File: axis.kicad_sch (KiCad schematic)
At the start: 43 parts, among them J101 CORTEX-DEBUG, J102 JAE_DX07S016JA3, SW101 SW_Push, SW102 SW_Push, U101 TPS78433QWDRBRQ1, U102 ATSAMD51G, U103 BMM150, U104 BHI160, Y101 32k768

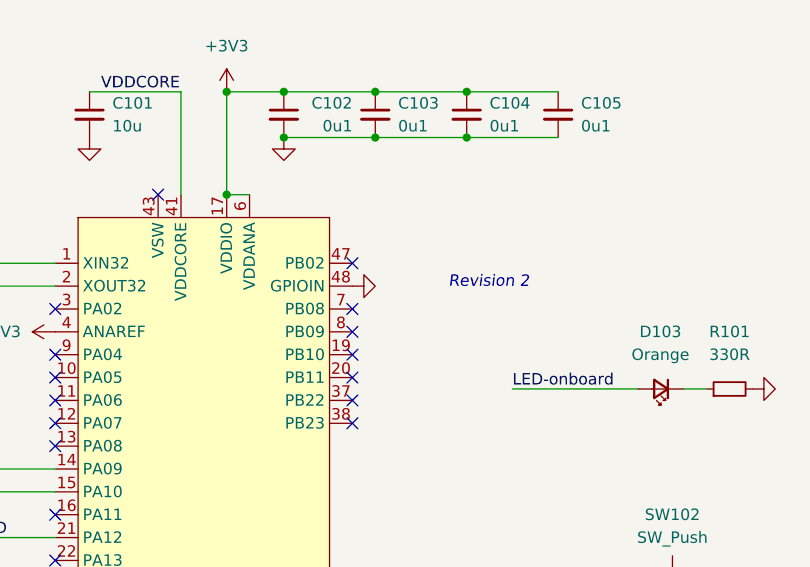
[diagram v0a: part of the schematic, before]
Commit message: Remove revision pin
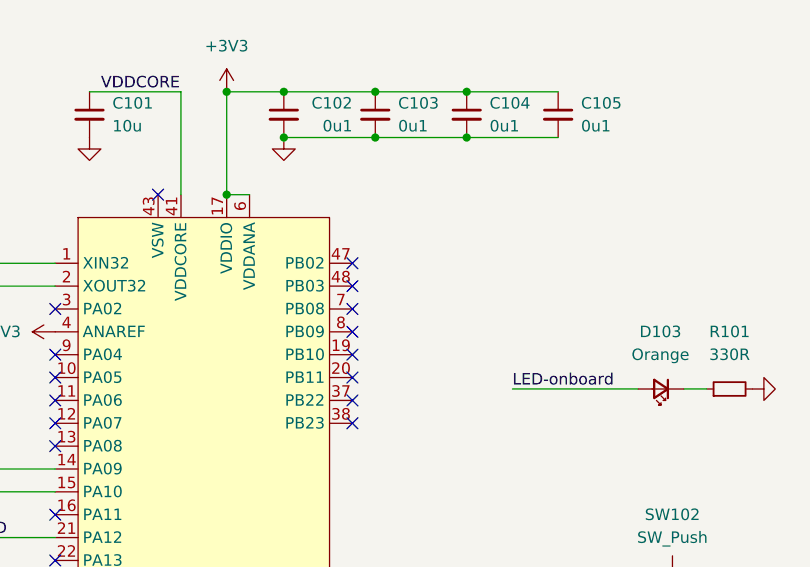
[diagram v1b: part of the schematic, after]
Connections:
- net GND: no longer U102.48 (PB03)
- no-connect marks 29 -> 30
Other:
- note removed: "Revision 2"
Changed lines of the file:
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@@
 		)
 	)
-	(text "Revision 2"
-		(exclude_from_sim no)
-		(at 103.3812 43.5526 0)
-		(effects
-			(font
-				(size 1.27 1.27)
-				(italic yes)
-			)
-			(justify left bottom)
-		)
-	)
 	(text "Mechanical / Production"
 		(exclude_from_sim no)
@@
 	)
 	(no_connect
+		(at 92.71 43.18)
+	)
+	(no_connect
 		(at 71.12 33.02)
 	)
@@
 	(symbol
 		(lib_id "power:GND")
-		(at 92.71 43.18 90)
-		(unit 1)
-		(exclude_from_sim no)
-		(in_bom yes)
-		(on_board yes)
-		(dnp no)
-		(property "Reference" "#PWR0107"
-			(at 99.06 43.18 0)
-			(effects
-				(font
-					(size 1.27 1.27)
-				)
-				(hide yes)
-			)
-		)
-		(property "Value" "GND"
-			(at 96.52 42.5449 90)
-			(effects
-				(font
-					(size 1.27 1.27)
-				)
-				(justify right)
-				(hide yes)
-			)
-		)
-		(property "Footprint" ""
-			(at 92.71 43.18 0)
-			(effects
-				(font
-					(size 1.27 1.27)
-				)
-				(hide yes)
-			)
-		)
-		(property "Datasheet" ""
-			(at 92.71 43.18 0)
-			(effects
-				(font
-					(size 1.27 1.27)
-				)
-				(hide yes)
-			)
-		)
-		(property "Description" ""
-			(at 92.71 43.18 0)
-			(effects
-				(font
-					(size 1.27 1.27)
-				)
-				(hide yes)
-			)
-		)
-		(pin "1"
-		)
-		(instances
-			(project "axis"
-				(path "/6c8448b4-b04d-47e1-934e-e40cbe27a7be"
-					(reference "#PWR0107")
-					(unit 1)
-				)
-			)
-		)
-	)
-	(symbol
-		(lib_id "power:GND")
 		(at 215.9 97.79 90)
 		(unit 1)
@@
 			)
 		)
+		(property "Sim.Pins" "1=K 2=A"
+			(at 127 54.61 0)
+			(effects
+				(font
+					(size 1.27 1.27)
+				)
+				(hide yes)
+			)
+		)
 		(pin "1"
 		)
@@
 		(at 205.74 157.48 90)
 		(unit 1)
-		(exclude_from_sim yes)
+		(exclude_from_sim no)
 		(in_bom no)
 		(on_board yes)
@@
 			)
 		)
+		(property "Sim.Enable" "0"
+			(at 205.74 157.48 0)
+			(effects
+				(font
+					(size 1.27 1.27)
+				)
+				(hide yes)
+			)
+		)
 		(instances
 			(project "axis"
@@
 		(at 247.65 151.13 0)
 		(unit 1)
-		(exclude_from_sim yes)
+		(exclude_from_sim no)
 		(in_bom no)
 		(on_board yes)
@@
 			)
 		)
+		(property "Sim.Enable" "0"
+			(at 247.65 151.13 0)
+			(effects
+				(font
+					(size 1.27 1.27)
+				)
+				(hide yes)
+			)
+		)
 		(instances
 			(project ""
@@
 		(at 125.73 101.6 0)
 		(unit 1)
-		(exclude_from_sim yes)
+		(exclude_from_sim no)
 		(in_bom no)
 		(on_board yes)
@@
 			)
 		)
+		(property "Sim.Enable" "0"
+			(at 125.73 101.6 0)
+			(effects
+				(font
+					(size 1.27 1.27)
+				)
+				(hide yes)
+			)
+		)
 		(pin "1"
 		)
@@
 		(at 180.34 189.23 0)
 		(unit 1)
-		(exclude_from_sim yes)
+		(exclude_from_sim no)
 		(in_bom no)
 		(on_board yes)
@@
 			)
 		)
+		(property "Sim.Enable" "0"
+			(at 180.34 189.23 0)
+			(effects
+				(font
+					(size 1.27 1.27)
+				)
+				(hide yes)
+			)
+		)
 		(instances
 			(project "axis"
@@
 		(at 232.41 157.48 0)
 		(unit 1)
-		(exclude_from_sim yes)
+		(exclude_from_sim no)
 		(in_bom no)
 		(on_board yes)
@@
 			)
 		)
+		(property "Sim.Enable" "0"
+			(at 232.41 157.48 0)
+			(effects
+				(font
+					(size 1.27 1.27)
+				)
+				(hide yes)
+			)
+		)
 		(instances
 			(project "axis"
@@
 		(at 134.62 171.45 0)
 		(unit 1)
-		(exclude_from_sim yes)
+		(exclude_from_sim no)
 		(in_bom yes)
 		(on_board yes)
@@
 			)
 		)
+		(property "Sim.Enable" "0"
+			(at 134.62 171.45 0)
+			(effects
+				(font
+					(size 1.27 1.27)
+				)
+				(hide yes)
+			)
+		)
 		(pin "A1"
 		)
@@
 		(at 276.86 154.94 0)
 		(unit 1)
-		(exclude_from_sim yes)
+		(exclude_from_sim no)
 		(in_bom no)
 		(on_board yes)
@@
 			)
 		)
+		(property "Sim.Enable" "0"
+			(at 276.86 154.94 0)
+			(effects
+				(font
+					(size 1.27 1.27)
+				)
+				(hide yes)
+			)
+		)
 		(instances
 			(project "axis"
@@
 		(at 276.86 166.37 0)
 		(unit 1)
-		(exclude_from_sim yes)
+		(exclude_from_sim no)
 		(in_bom no)
 		(on_board yes)
@@
 			)
 		)
+		(property "Sim.Enable" "0"
+			(at 276.86 166.37 0)
+			(effects
+				(font
+					(size 1.27 1.27)
+				)
+				(hide yes)
+			)
+		)
 		(instances
 			(project "axis"
@@
 		(at 49.53 173.99 0)
 		(unit 1)
-		(exclude_from_sim yes)
+		(exclude_from_sim no)
 		(in_bom yes)
 		(on_board yes)
@@
 			)
 		)
+		(property "Sim.Enable" "0"
+			(at 49.53 173.99 0)
+			(effects
+				(font
+					(size 1.27 1.27)
+				)
+				(hide yes)
+			)
+		)
 		(pin "1"
 		)
@@
 		(at 186.69 105.41 0)
 		(unit 1)
-		(exclude_from_sim yes)
+		(exclude_from_sim no)
 		(in_bom yes)
 		(on_board yes)
@@
 			)
 		)
+		(property "Sim.Enable" "0"
+			(at 186.69 105.41 0)
+			(effects
+				(font
+					(size 1.27 1.27)
+				)
+				(hide yes)
+			)
+		)
 		(pin "A5"
 		)
@@
 		(at 247.65 158.75 0)
 		(unit 1)
-		(exclude_from_sim yes)
+		(exclude_from_sim no)
 		(in_bom no)
 		(on_board yes)
@@
 			)
 		)
+		(property "Sim.Enable" "0"
+			(at 247.65 158.75 0)
+			(effects
+				(font
+					(size 1.27 1.27)
+				)
+				(hide yes)
+			)
+		)
 		(instances
 			(project "axis"
@@
 		(at 276.86 177.8 0)
 		(unit 1)
-		(exclude_from_sim yes)
+		(exclude_from_sim no)
 		(in_bom no)
 		(on_board yes)
@@
 			)
 		)
+		(property "Sim.Enable" "0"
+			(at 276.86 177.8 0)
+			(effects
+				(font
+					(size 1.27 1.27)
+				)
+				(hide yes)
+			)
+		)
 		(instances
 			(project "axis"
@@
 		)
 		(pin "48"
-			(alternate "GPIOIN")
 		)
 		(pin "49"
@@
 		(at 179.07 175.26 0)
 		(unit 1)
-		(exclude_from_sim yes)
+		(exclude_from_sim no)
 		(in_bom no)
 		(on_board yes)
@@
 			)
 		)
+		(property "Sim.Enable" "0"
+			(at 179.07 175.26 0)
+			(effects
+				(font
+					(size 1.27 1.27)
+				)
+				(hide yes)
+			)
+		)
 		(instances
 			(project "axis"
@@
 		(at 180.34 156.21 0)
 		(unit 1)
-		(exclude_from_sim yes)
+		(exclude_from_sim no)
 		(in_bom no)
 		(on_board yes)
@@
 			(at 180.34 156.21 0)
 			(effects
+				(font
+					(size 1.27 1.27)
+				)
+				(hide yes)
+			)
+		)
+		(property "Sim.Enable" "0"
+			(at 180.34 156.21 0)
+			(effects
